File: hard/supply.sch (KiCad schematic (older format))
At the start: 14 parts, among them J2 MicroXNJ

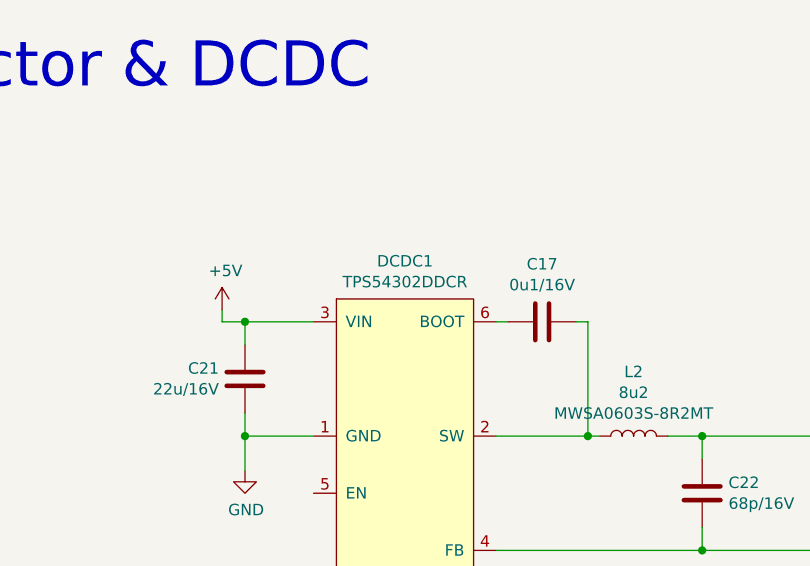
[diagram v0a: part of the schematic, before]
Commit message: updated dcdc + usb jack.
release candidate, ready for review by @lukekaese
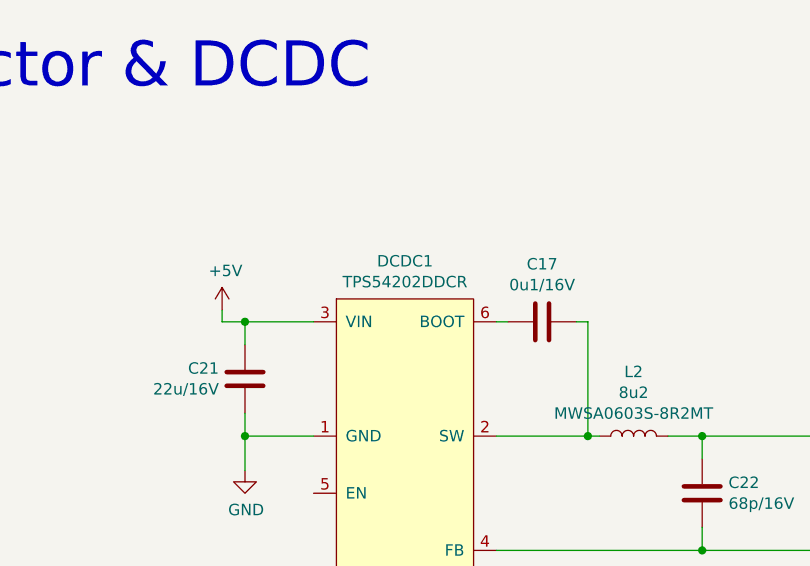
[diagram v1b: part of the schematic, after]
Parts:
- removed DCDC1: TPS54302DDCR, Package_TO_SOT_SMD:SOT-23-6_Handsoldering, symbol led_matrix:TPS54302DDCR
- added DCDC1: TPS54202DDCR, Package_TO_SOT_SMD:SOT-23-6_Handsoldering, symbol led_matrix:TPS54202DDCR
- J2: footprint led_matrix:Connectors_SHOU-HAN_MICRO-4P-DIP -> led_matrix:Connectors_SHOU-HAN_MicroXNJ; Description USB CONNECTORS ROHS -> SMD USB CONNECTORS ROHS; LCSC C456008 -> C404969; MPN MICRO 4P DIP -> MicroXNJ
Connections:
- net +5V: now also DCDC1.3 (VIN)
- net GND: now also DCDC1.1 (GND)
- net at C17.1, L2.1: now also DCDC1.2 (SW)
- net at C17.2: now also DCDC1.6 (BOOT)
- net at C22.1, R199.2, R200.1: now also DCDC1.4 (FB)
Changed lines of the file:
@@
 $EndDescr
-$Comp
-L led_matrix:TPS54302DDCR DCDC1
-U 1 1 6056940B
-P 6550 3300
-F 0 "DCDC1" H 6550 3465 50  0000 C CNN
-F 1 "TPS54302DDCR" H 6550 3374 50  0000 C CNN
-F 2 "Package_TO_SOT_SMD:SOT-23-6_Handsoldering" H 6550 3300 50  0001 C CNN
-F 3 "https://www.ti.com/lit/gpn/TPS54302" H 6550 3300 50  0001 C CNN
-F 4 "296-46237-1-ND" H 6550 3300 50  0001 C CNN "DigiKey"
-F 5 "C311983" H 6550 3300 50  0001 C CNN "LCSC"
-F 6 "Texas Instruments" H 6550 3300 50  0001 C CNN "MF"
-F 7 "TPS54302DDCR" H 6550 3300 50  0001 C CNN "MPN"
-F 8 "IC REG BUCK ADJ 3A TSOT23-6" H 6550 3300 50  0001 C CNN "Description"
-	1    6550 3300
-	1    0    0    -1
-$EndComp
 $Comp
 L Device:C C21
@@
 F 0 "J2" H 2507 4067 50  0000 C CNN
 F 1 "MicroXNJ" H 2507 3976 50  0000 C CNN
-F 2 "led_matrix:Connectors_SHOU-HAN_MICRO-4P-DIP" H 2600 3550 50  0001 C CNN
-F 3 "https://datasheet.lcsc.com/szlcsc/1912111437_SHOU-HAN-MICRO-4P-DIP_C456008.pdf" H 2600 3550 50  0001 C CNN
+F 2 "led_matrix:Connectors_SHOU-HAN_MicroXNJ" H 2600 3550 50  0001 C CNN
+F 3 "https://datasheet.lcsc.com/szlcsc/1912111437_SHOU-HAN-MicroXNJ_C404969.pdf" H 2600 3550 50  0001 C CNN
 F 4 "" H 2450 3600 50  0001 C CNN "DigiKey"
 F 5 "" H 2450 3600 50  0001 C CNN "Mouser"
-F 6 "C456008" H 2450 3600 50  0001 C CNN "LCSC"
+F 6 "C404969" H 2450 3600 50  0001 C CNN "LCSC"
 F 7 "SHOU HAN" H 2450 3600 50  0001 C CNN "MF"
-F 8 "MICRO 4P DIP" H 2450 3600 50  0001 C CNN "MPN"
-F 9 "USB CONNECTORS ROHS" H 2450 3600 50  0001 C CNN "Description"
+F 8 "MicroXNJ" H 2450 3600 50  0001 C CNN "MPN"
+F 9 "SMD USB CONNECTORS ROHS" H 2450 3600 50  0001 C CNN "Description"
 	1    2450 3600
 	1    0    0    -1
@@
 	0    1    -1   0
 $EndComp
+$Comp
+L led_matrix:TPS54202DDCR DCDC1
+U 1 1 605E86F2
+P 6550 3300
+F 0 "DCDC1" H 6550 3465 50  0000 C CNN
+F 1 "TPS54202DDCR" H 6550 3374 50  0000 C CNN
+F 2 "Package_TO_SOT_SMD:SOT-23-6_Handsoldering" H 6550 3300 50  0001 C CNN
+F 3 "https://www.ti.com/lit/ds/symlink/tps54202.pdf" H 6550 3300 50  0001 C CNN
+F 4 "296-TPS54202DDCRCT-ND" H 6550 3300 50  0001 C CNN "DigiKey"
+F 5 "C191884" H 6550 3300 50  0001 C CNN "LCSC"
+F 6 "Texas Instruments" H 6550 3300 50  0001 C CNN "MF"
+F 7 "TPS54202DDCR" H 6550 3300 50  0001 C CNN "MPN"
+F 8 "IC REG BUCK ADJ 2A TSOT23-6" H 6550 3300 50  0001 C CNN "Description"
+	1    6550 3300
+	1    0    0    -1
+$EndComp
 $EndSCHEMATC
